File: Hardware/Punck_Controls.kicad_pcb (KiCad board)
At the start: 2 copper layers, 91.3 x 110 mm, 36 parts, among them J1 Conn_01x12_Female, J10 Audio_Out_R, J11 USB_B_Micro, J12 Midi_In_L, J13 Audio_Out_L, J2 Conn_01x12_Female, J3 Conn_01x12_Female, J4 Kick_In, J5 Snare_In, J6 CH_In, J7 SamplerA_In, J8 SamplerB_In, J9 Conn_01x12_Female

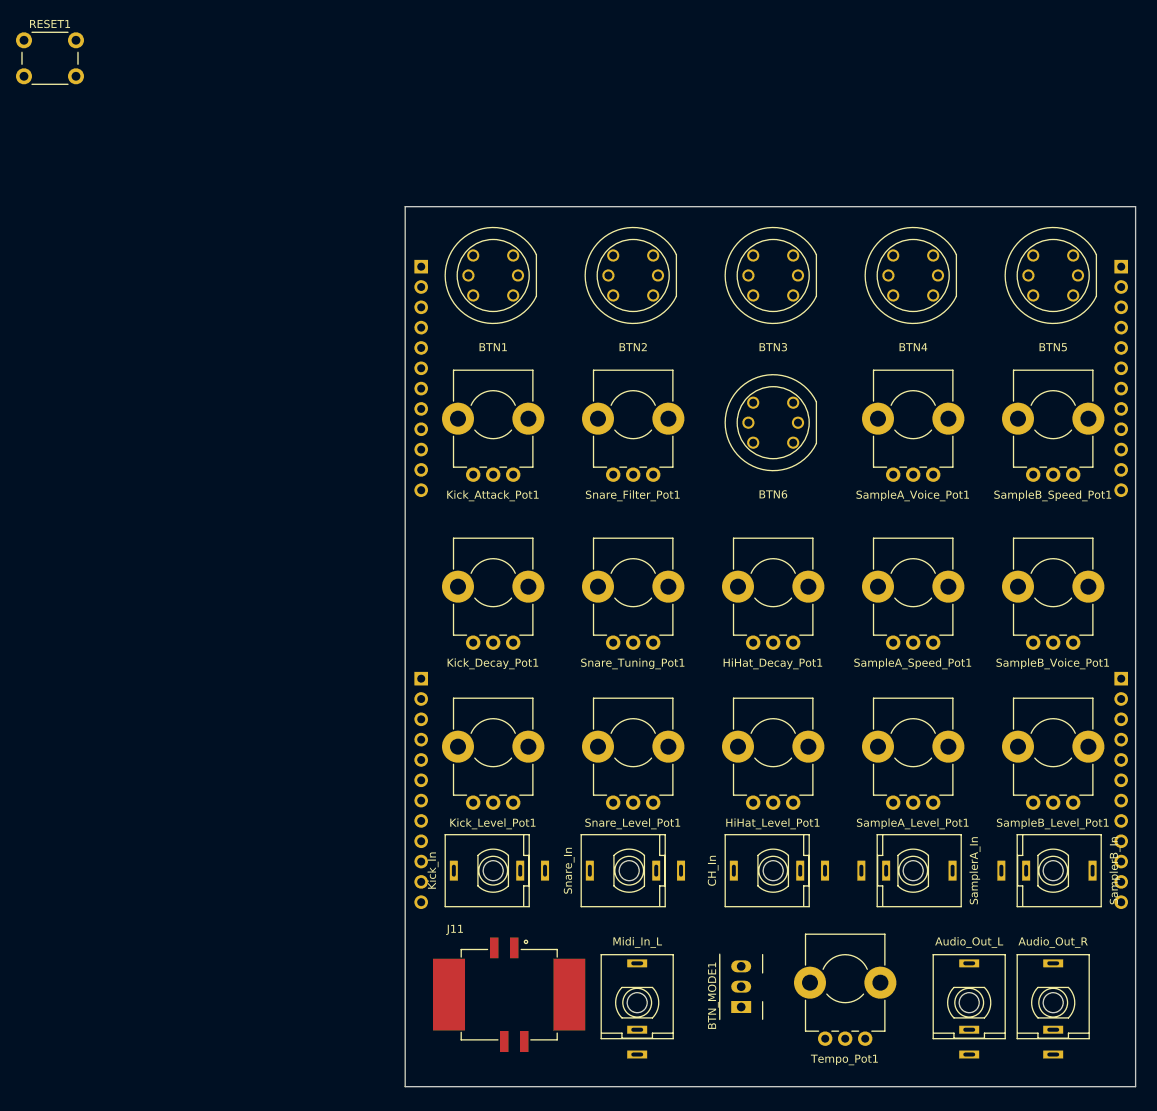
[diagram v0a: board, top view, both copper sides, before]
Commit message: First draft of Controls PCB
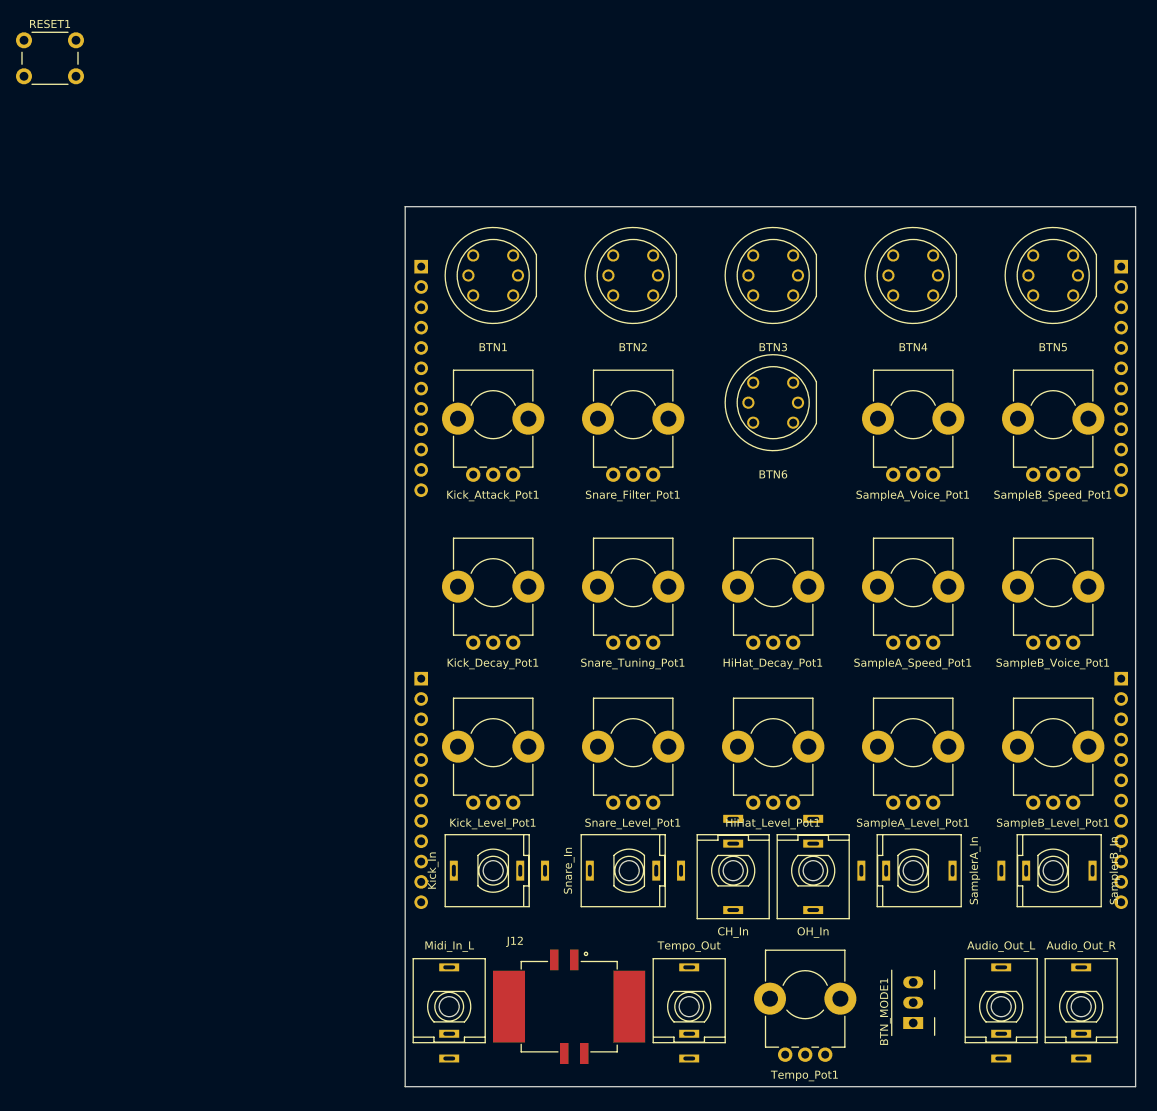
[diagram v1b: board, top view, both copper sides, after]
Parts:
- added J15: Audio_Out_R, Custom_Footprints:THONKICONN_hole, F.Cu at (154.5, 150.0)
- added J7: OH_In, Custom_Footprints:THONKICONN_hole, F.Cu at (121.0, 133.0)
- J11: renamed from J10; value Audio_Out_R -> Tempo_Out
- moved J11 45.5 mm to (105.5, 150.0)
- moved J13 23.5 mm to (75.5, 150.0)
- moved BTN_MODE1 21.6 mm to (133.5, 149.5)
- moved J12 7.65 mm to (90.5, 150.0)
- moved Tempo_Pot1 5.39 mm to (120.0, 148.5)
- moved J6 5.00 mm to (111.0, 133.0), turned to 180 degrees
- moved J14 4.03 mm to (144.5, 150.0)
- moved BTN6 2.50 mm to (116.0, 74.5)
- renumbered J9 to J10, J11 to J12, J12 to J13, J13 to J14, J7 to J8, J8 to J9
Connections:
- net /EXT_AUDIO_OUT_L renamed /AUDIO_OUT_L
- net /OH_IN renamed /CH_IN
- net /TEMPO renamed /TEMPO_POT
- J1 pad 12: unconnected-(J1-Pad12) -> GND
- J10 pad 10: /EXT_AUDIO_OUT_R -> /AUDIO_OUT_R
- J11 pad 3: /EXT_AUDIO_OUT_R -> /TEMPO_OUT
- J2 pad 1: unconnected-(J2-Pad1) -> +3.3VA
- J2 pad 12: unconnected-(J2-Pad12) -> GND
- J3 pad 1: unconnected-(J3-Pad1) -> +3.3VA
- J3 pad 11: unconnected-(J3-Pad11) -> /TEMPO_OUT
- J3 pad 12: unconnected-(J3-Pad12) -> GND

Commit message: Component PCB Signal routing first draft
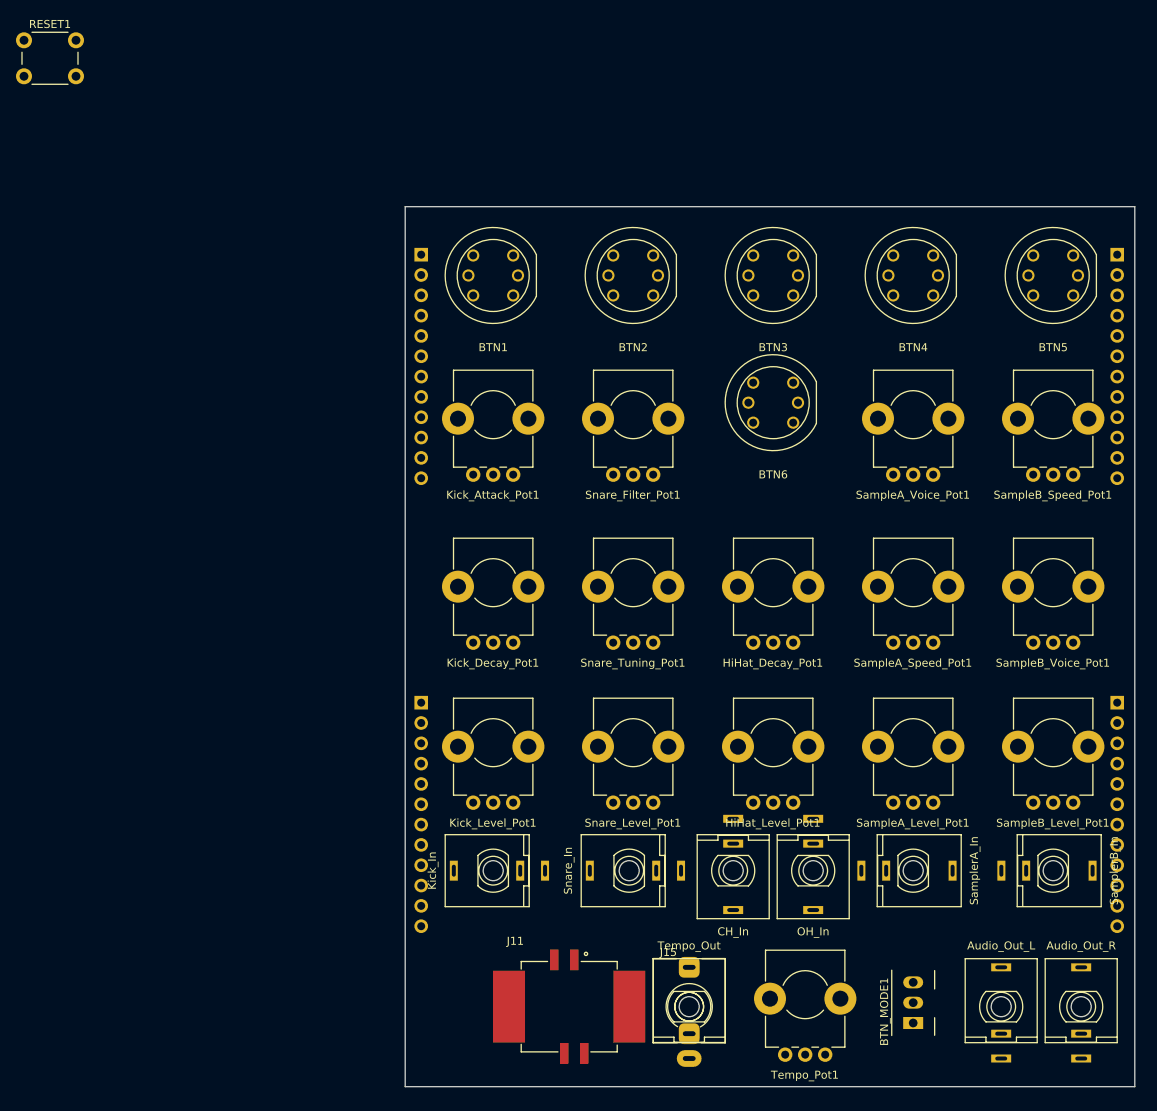
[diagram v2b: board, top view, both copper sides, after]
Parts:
- removed the J13 at (75.5, 150.0)
- added J15: Midi_In, Custom_Footprints:Thonkiconn_Stereo-PJ366ST, F.Cu at (105.5, 150.0)
- moved J10 87.6 mm to (72.0, 112.0)
- moved J3 87.5 mm to (72.0, 56.0)
- moved J2 87.1 mm to (159.0, 112.0)
- moved J1 87.0 mm to (159.0, 56.0)
- renumbered J12 to J11, J11 to J12, J14 to J13, J15 to J14
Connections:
- J10 pad 1: unconnected-(J10-Pad1) -> +3.3VA
- J2 pad 1: +3.3VA -> /KI_BTN
- J2 pad 10: /SNARE_VOL_POT -> /SNARE_TUNING_POT
- J2 pad 11: unconnected-(J2-Pad11) -> /SNARE_VOL_POT
- J2 pad 2: /CH_IN -> /KI_LED
- J2 pad 3: /SB_BTN -> /CH_IN
- J2 pad 4: /SB_LED -> /SB_BTN
- J2 pad 5: /KICK_ATTACK_POT -> /SB_LED
- J2 pad 6: /KICK_DECAY_POT -> /KICK_ATTACK_POT
- J2 pad 7: /KICK_VOL_POT -> /KICK_DECAY_POT
- J2 pad 8: /SNARE_FILTER_POT -> /KICK_VOL_POT
- J2 pad 9: /SNARE_TUNING_POT -> /SNARE_FILTER_POT
- J3 pad 1: +3.3VA -> /OH_IN
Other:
- board size 91.3 x 110 mm -> 91.2 x 110 mm

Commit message: Component PCB first draft
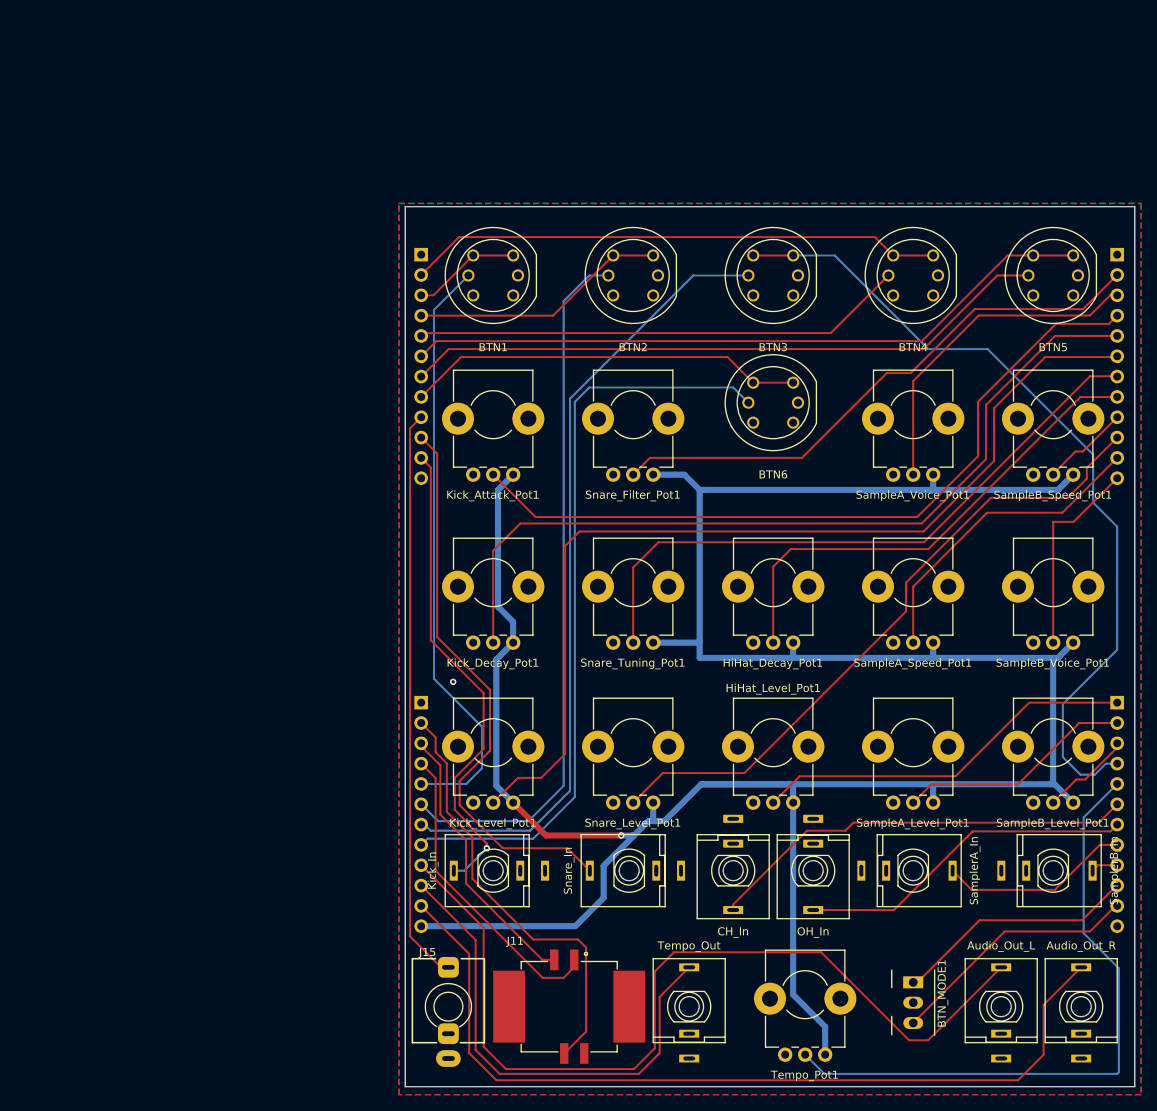
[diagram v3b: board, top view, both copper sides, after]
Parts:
- removed RESET1: SW_Push, Custom_Footprints:SW_PUSH_6mm_aligned
- moved J15 30.1 mm to (75.4, 150.0)
- turned BTN_MODE1 to -90 degrees
- renumbered J4 to J10, J10 to J4
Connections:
- J1 pad 1: +3.3VA -> GND
- J1 pad 10: /SA_LED -> /SNARE_VOL_POT
- J1 pad 11: /SNARE_IN -> /SAMPLER_A_SPEED_POT
- J1 pad 12: GND -> /SAMPLER_B_VOICE_POT
- J1 pad 2: /KICK_IN -> /SNARE_FILTER_POT
- J1 pad 3: /SN_BTN -> /SAMPLER_A_VOICE_POT
- J1 pad 4: /SN_LED -> /KICK_ATTACK_POT
- J1 pad 5: /OH_BTN -> /KICK_DECAY_POT
- J1 pad 6: /OH_LED -> /KICK_VOL_POT
- J1 pad 7: /CH_BTN -> /SNARE_TUNING_POT
- J1 pad 8: /CH_LED -> /HIHAT_DECAY_POT
- J1 pad 9: /SA_BTN -> /SAMPLER_B_SPEED_POT
- J2 pad 1: /KI_BTN -> /HIHAT_VOL_POT
- J2 pad 10: /SNARE_TUNING_POT -> /MIDI_LEARN
- J2 pad 11: /SNARE_VOL_POT -> /SEQ_SELECT
- J2 pad 2: /KI_LED -> /SAMPLER_A_VOL_POT
- J2 pad 3: /CH_IN -> /SAMPLER_B_VOL_POT
- J2 pad 4: /SB_BTN -> /CH_BTN
- J2 pad 5: /SB_LED -> /TEMPO_POT
- J2 pad 6: /KICK_ATTACK_POT -> /CH_IN
- J2 pad 7: /KICK_DECAY_POT -> /OH_IN
- J2 pad 8: /KICK_VOL_POT -> /SAMPLER_A_IN
- J2 pad 9: /SNARE_FILTER_POT -> /SAMPLER_B_IN
- J3 pad 1: /OH_IN -> GND
- J3 pad 10: /SAMPLER_B_VOL_POT -> /SNARE_IN
- J3 pad 11: /TEMPO_OUT -> /KICK_IN
- J3 pad 2: /SAMPLERA_IN -> /SA_BTN
- J3 pad 3: /HIHAT_DECAY_POT -> /KI_BTN
- J3 pad 4: /HIHAT_VOL_POT -> /SN_BTN
- J3 pad 5: /SAMPLER_A_VOICE_POT -> /SA_LED
- J3 pad 6: /SAMPLER_A_SPEED_POT -> /SB_BTN
- J3 pad 7: /SAMPLER_A_VOL_POT -> /SB_LED
- J3 pad 8: /SAMPLER_B_VOICE_POT -> /OH_BTN
- J3 pad 9: /SAMPLER_B_SPEED_POT -> /MIDI_IN
- J4 pad 1: +3.3VA -> GND
- J4 pad 10: /AUDIO_OUT_R -> /TEMPO_OUT
- J4 pad 11: /AUDIO_OUT_L -> /AUDIO_OUT_R
- J4 pad 12: GND -> +3.3VA
- J4 pad 2: /SAMPLERB_IN -> /USB_DP
- J4 pad 3: /USB_DP -> /USB_DM
- J4 pad 4: /USB_DM -> /USB_VBUS
- J4 pad 5: /USB_VBUS -> /KI_LED
- J4 pad 6: /MIDI_IN -> /SN_LED
- J4 pad 7: /MIDI_LEARN -> /CH_LED
- J4 pad 8: /SEQ_SELECT -> /OH_LED
- J4 pad 9: /TEMPO_POT -> /AUDIO_OUT_L
- J8 pad 3: /SAMPLERA_IN -> /SAMPLER_A_IN
- J9 pad 3: /SAMPLERB_IN -> /SAMPLER_B_IN
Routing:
- net +3.3VA: track 0.00 -> 354.4 mm, vias 0 -> 1
- net /KICK_VOL_POT: track 0.00 -> 120.2 mm
- net /AUDIO_OUT_L: track 0.00 -> 111.8 mm
- net /AUDIO_OUT_R: track 0.00 -> 108.3 mm
- net /KICK_DECAY_POT: track 0.00 -> 104.6 mm
- net /CH_BTN: track 0.00 -> 103.0 mm
- net /CH_LED: track 0.00 -> 98.7 mm
- net /KICK_ATTACK_POT: track 0.00 -> 94.6 mm
- net /OH_LED: track 0.00 -> 94.3 mm
- net /SN_LED: track 0.00 -> 88.0 mm
- net /SB_BTN: track 0.00 -> 86.7 mm
- net /SNARE_VOL_POT: track 0.00 -> 82.3 mm
- net /SB_LED: track 0.00 -> 81.1 mm
- net /TEMPO_POT: track 0.00 -> 79.9 mm
- net /SNARE_TUNING_POT: track 0.00 -> 79.8 mm
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- added copper zone on B.Cu, net GND
- added copper zone on F.Cu, net GND

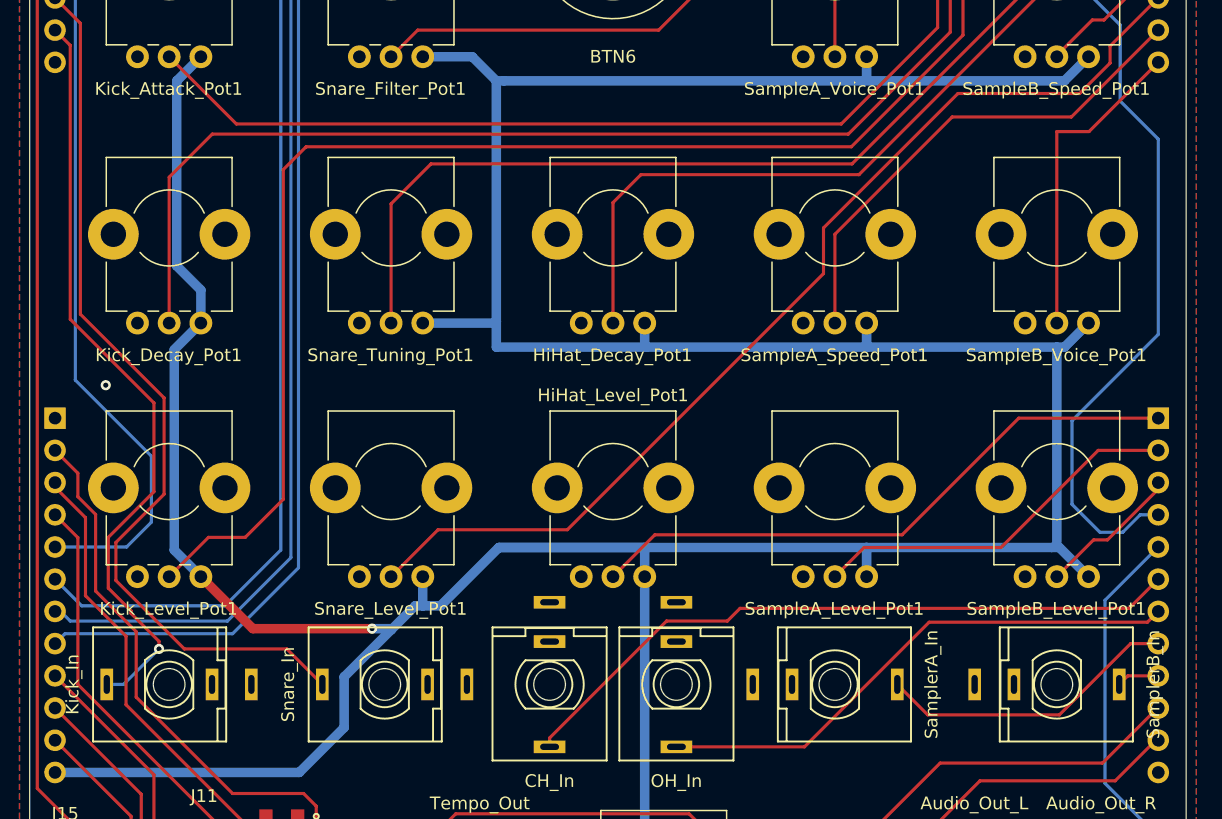
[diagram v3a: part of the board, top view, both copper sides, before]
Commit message: Started panel layout
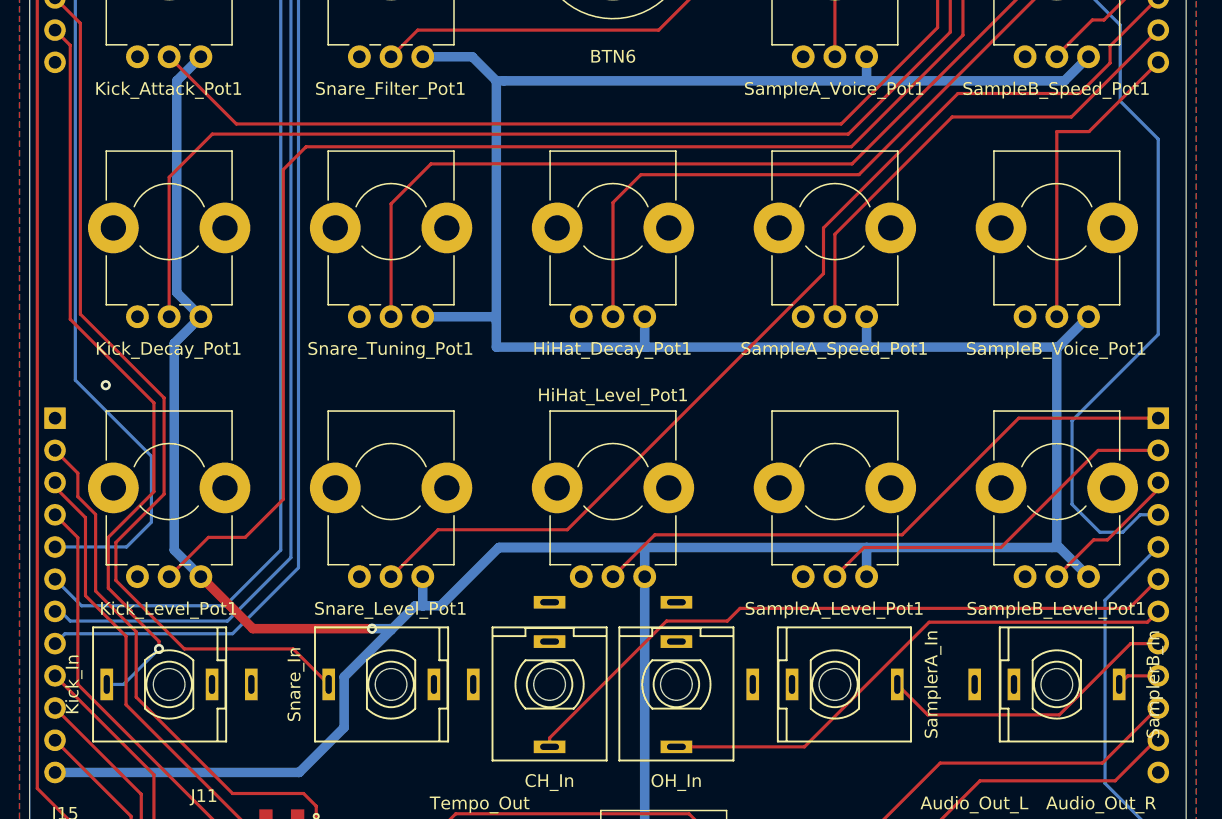
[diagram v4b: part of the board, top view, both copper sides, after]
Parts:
- moved HiHat_Decay_Pot1 0.50 mm to (116.0, 96.5)
- moved J5 0.50 mm to (98.5, 133.0)
- moved Kick_Decay_Pot1 0.50 mm to (81.0, 96.5)
- moved SampleA_Speed_Pot1 0.50 mm to (133.5, 96.5)
- moved SampleB_Voice_Pot1 0.50 mm to (151.0, 96.5)
- moved Snare_Tuning_Pot1 0.50 mm to (98.5, 96.5)
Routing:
- net +3.3VA: track 354.4 -> 355.4 mm
- net /KICK_DECAY_POT: track 104.6 -> 104.1 mm
- net /SNARE_TUNING_POT: track 79.8 -> 79.3 mm
- net /SNARE_IN: track 70.8 -> 71.3 mm
- net /SAMPLER_B_VOICE_POT: track 25.4 -> 24.9 mm
- net /SAMPLER_A_SPEED_POT: track 39.2 -> 38.7 mm
